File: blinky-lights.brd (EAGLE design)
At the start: 63.5 x 63.5 mm, 20 parts, among them Q1 N3, U1 555, U2 A2678EAT

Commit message: board layout
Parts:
- C1: value 10n -> 0.01u
- C3: value 100u -> 10u
- LED0, LED1, LED2, LED3, LED4, LED5, LED6, LED7: device led:LED5MM -> led:LED3MM
- Q1: value N3 -> NFET
- R4: value 1k -> 50
- R5: value 10k -> 1k
- moved C3 37.0 mm to (15.2, 6.99)
- moved JP1 30.6 mm to (15.2, 14.0), turned to 0 degrees
- moved Q1 29.8 mm to (6.35, 40.0), turned to 90 degrees
- moved C1 23.8 mm to (28.6, 33.0), turned to 0 degrees
- moved R3 19.9 mm to (29.2, 20.3), turned to 90 degrees
- moved R1 14.4 mm to (10.8, 24.8), turned to 270 degrees
- moved LED3 12.6 mm to (47.0, 47.0), turned to 180 degrees
- moved LED2 10.9 mm to (25.4, 47.0)
- moved LED4 10.9 mm to (47.0, 25.4), turned to 180 degrees
- moved C2 10.4 mm to (21.0, 15.9)
- moved U2 10.2 mm to (36.8, 33.0), turned to 90 degrees
- moved LED1 9.67 mm to (3.81, 47.0)
- moved LED5 9.67 mm to (47.0, 3.81), turned to 180 degrees
- moved U1 7.43 mm to (20.3, 24.8), turned to 0 degrees
- moved LED0 7.41 mm to (3.81, 25.4)
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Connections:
- removed net DATA: Q1.E, R4.2, U2.2
- removed net N$12: Q1.B, R5.2
- removed net N$13: C3.A, JP1.1
- new net N$5: Q1.S, R4.2, U2.6
- new net SENSE: LED1.K, Q1.G, R4.1
- net FEEDBACK: now also Q1.D, R5.2, U2.2; no longer LED1.K, R5.1, U2.6
- net GND: now also JP1.1; no longer R4.1
- net VCC: now also C3.A, R5.1; no longer Q1.C
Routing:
- net VCC: track 0.00 -> 249.6 mm
- net FEEDBACK: track 0.00 -> 67.0 mm
- net N$1: track 0.00 -> 59.7 mm
- net N$4: track 0.00 -> 59.5 mm
- net CLK: track 0.00 -> 47.8 mm
- net N$5: track 0.00 -> 47.5 mm
- net N$7: track 0.00 -> 46.4 mm
- net N$8: track 0.00 -> 42.1 mm
- net GND: track 0.00 -> 39.2 mm, vias 0 -> 2
- net N$3: track 0.00 -> 26.2 mm
- net N$2: track 0.00 -> 20.1 mm
- net SENSE: track 0.00 -> 19.6 mm
- net N$11: track 0.00 -> 19.4 mm
- net N$9: track 0.00 -> 12.6 mm
- net N$6: track 0.00 -> 9.42 mm
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- added copper zone on layer 16, net GND
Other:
- board size 63.5 x 63.5 mm -> 50.8 x 50.8 mm

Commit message: minor cleanup on board
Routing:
- net GND: track 39.2 -> 18.4 mm
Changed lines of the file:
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@@
 <vertex x="50.8" y="0"/>
 </polygon>
-<wire x1="40.64" y1="24.13" x2="40.64" y2="12.065" width="0.4064" layer="16"/>
-<wire x1="40.64" y1="12.065" x2="42.545" y2="10.16" width="0.4064" layer="16"/>
 <via x="42.545" y="10.16" extent="1-16" drill="0.7" shape="octagon"/>
 <wire x1="42.545" y1="10.16" x2="24.13" y2="10.16" width="0.4064" layer="1"/>
 <via x="24.13" y="10.16" extent="1-16" drill="0.7" shape="octagon"/>
-<wire x1="24.13" y1="10.16" x2="24.13" y2="11.7" width="0.4064" layer="16"/>
-<wire x1="24.13" y1="11.7" x2="20.955" y2="14.875" width="0.4064" layer="16"/>
 </signal>
 <signal name="N$9">

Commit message: schematic and board clean up
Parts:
- R4: value 50 -> 10
- moved C3 5.39 mm to (19.1, 10.8), turned to 270 degrees
- moved R4 3.18 mm to (17.1, 38.7)
- moved JP1 2.84 mm to (14.0, 11.4)
- moved C2 2.01 mm to (22.9, 16.5)
- moved Q1 0.64 mm to (6.35, 39.4)
- moved C1 0.63 mm to (28.6, 33.7)
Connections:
- net SENSE: no longer Q1.G
- net VCC: now also Q1.G
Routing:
- net VCC: track 249.6 -> 255.7 mm
- net SENSE: track 19.6 -> 15.0 mm
- net GND: track 18.4 -> 16.5 mm
- net N$5: track 47.5 -> 46.1 mm
- net FEEDBACK: track 67.0 -> 68.4 mm
- net N$11: track 19.4 -> 20.5 mm
- net N$10: track 6.40 -> 7.25 mm
- net N$4: track 59.5 -> 58.7 mm

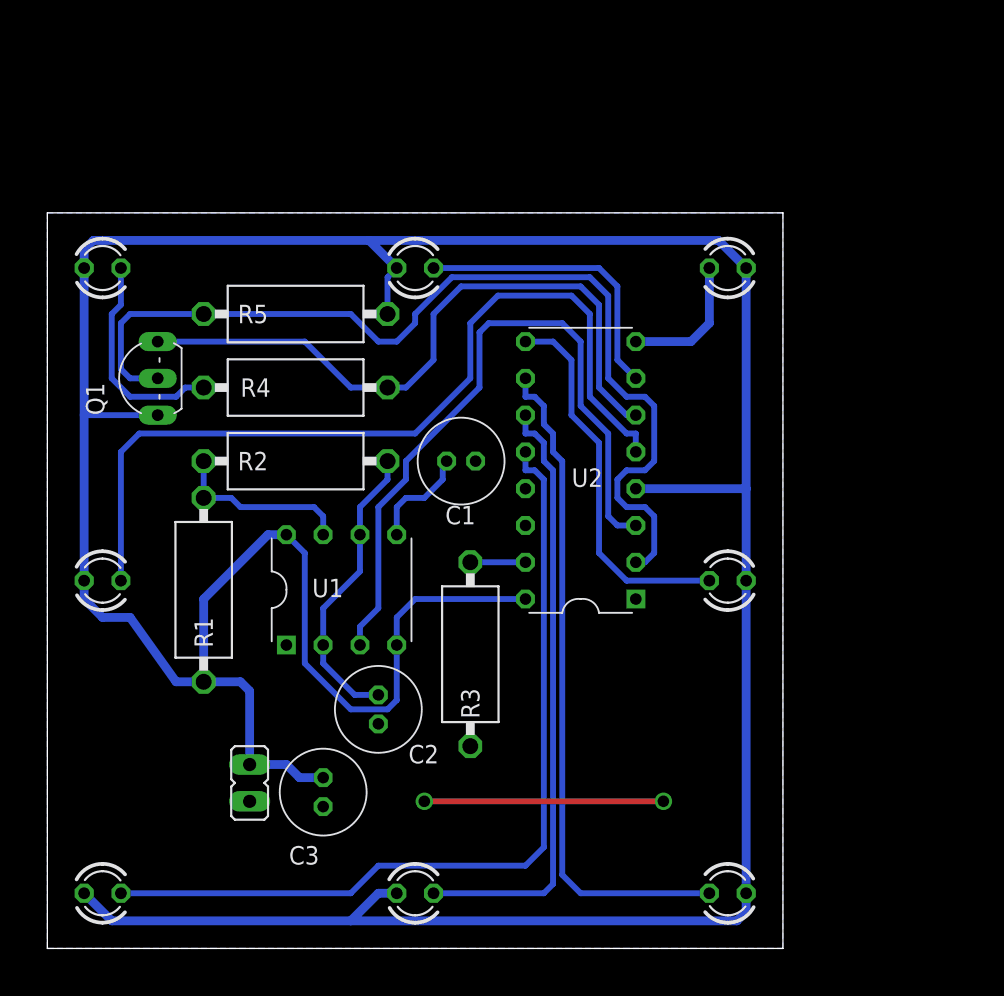
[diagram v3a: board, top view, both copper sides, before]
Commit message: board clean up, got rid of last airwire
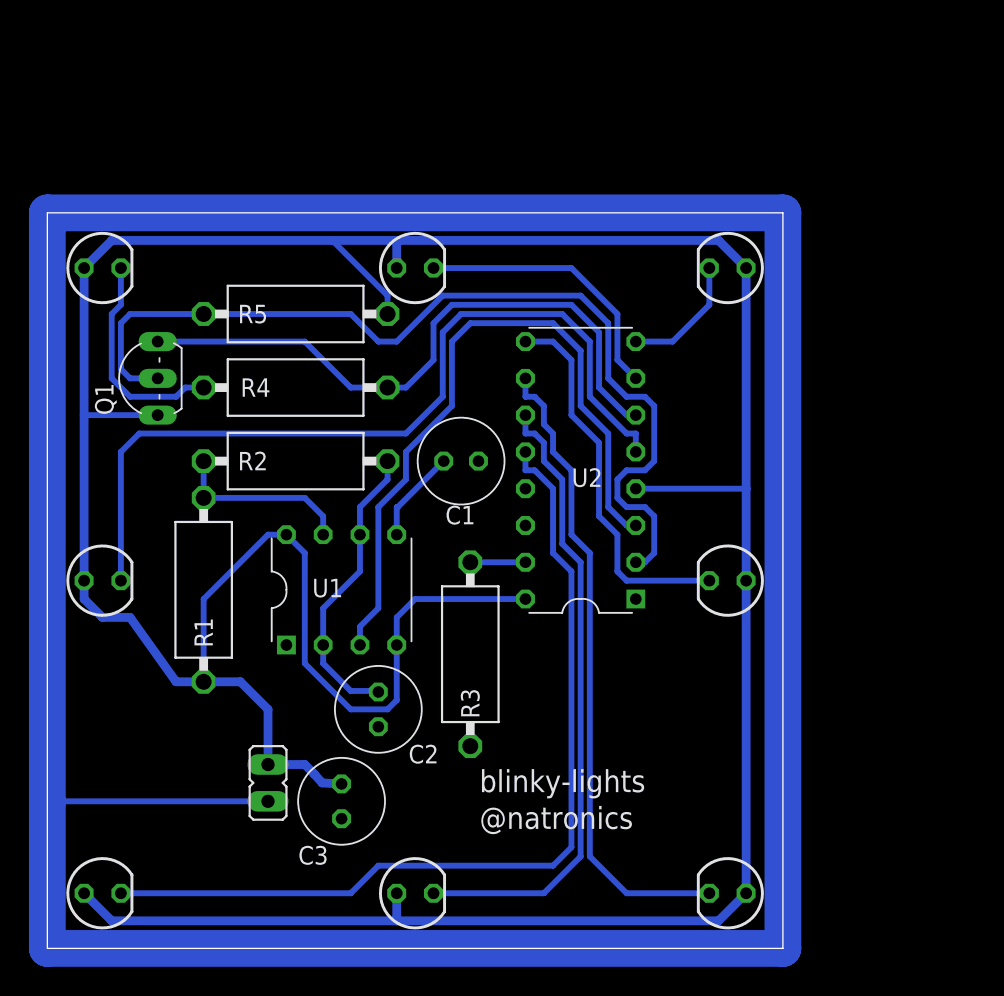
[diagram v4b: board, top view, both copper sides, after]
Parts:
- LED0, LED1, LED2, LED3, LED4, LED5, LED6, LED7: value (none) -> LED3MM; device led:LED3MM -> blinky-lights:LED3MM
- moved C3 1.42 mm to (20.3, 10.2)
- moved JP1 1.27 mm to (15.2, 11.4)
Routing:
- net GND: track 16.5 -> 218.4 mm, vias 2 -> 0
- net N$4: track 58.7 -> 61.4 mm
- net FEEDBACK: track 68.4 -> 65.8 mm
- net N$5: track 46.1 -> 43.6 mm
- net N$7: track 46.4 -> 44.5 mm
- net N$1: track 59.7 -> 57.9 mm
- net N$8: track 42.1 -> 43.6 mm
- net N$2: track 20.1 -> 19.0 mm
- net N$10: track 7.25 -> 6.47 mm
- net N$6: track 9.42 -> 8.67 mm
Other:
- board text added: "@natronics"
- board text added: "blinky-lights"

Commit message: board and schematic cleanup
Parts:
- JP1: device jumper:JP1 -> blinky-lights:JP1
- R1, R2, R3, R4, R5: device rcl:VMTB60 -> blinky-lights:V234/12
